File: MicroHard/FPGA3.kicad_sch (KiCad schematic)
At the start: 19 parts, among them J7 FPGA_DEBUG, U4 XC7A100T-FTG256

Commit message: Initial layout
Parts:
- renumbered R20 to R16, R22 to R17, R23 to R18, R24 to R19, R21 to R20, R16 to R21, R17 to R22, R18 to R23, R19 to R24, TP2 to TP1, TP1 to TP2
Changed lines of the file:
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@@
 		(dnp no)
 		(fields_autoplaced yes)
-		(property "Reference" "R22"
+		(property "Reference" "R17"
 			(at 177.8 55.8799 0)
 			(effects
@@
 			(project ""
 				(path "/578bd531-a491-4b15-a479-460d159ffc14/e381883e-e672-4900-88a5-08b94f970a88/5897012d-c01f-459a-b65a-eba111a7dafb"
-					(reference "R22")
+					(reference "R17")
 					(unit 1)
 				)
@@
 		(dnp no)
 		(fields_autoplaced yes)
-		(property "Reference" "R20"
+		(property "Reference" "R16"
 			(at 153.67 52.0699 0)
 			(effects
@@
 			(project ""
 				(path "/578bd531-a491-4b15-a479-460d159ffc14/e381883e-e672-4900-88a5-08b94f970a88/5897012d-c01f-459a-b65a-eba111a7dafb"
-					(reference "R20")
+					(reference "R16")
 					(unit 1)
 				)
@@
 		(dnp no)
 		(fields_autoplaced yes)
-		(property "Reference" "R23"
+		(property "Reference" "R18"
 			(at 237.49 57.1499 0)
 			(effects
@@
 			(project ""
 				(path "/578bd531-a491-4b15-a479-460d159ffc14/e381883e-e672-4900-88a5-08b94f970a88/5897012d-c01f-459a-b65a-eba111a7dafb"
-					(reference "R23")
+					(reference "R18")
 					(unit 1)
 				)
@@
 		(dnp no)
 		(fields_autoplaced yes)
-		(property "Reference" "R16"
+		(property "Reference" "R21"
 			(at 49.53 123.19 90)
 			(effects
@@
 			(project ""
 				(path "/578bd531-a491-4b15-a479-460d159ffc14/e381883e-e672-4900-88a5-08b94f970a88/5897012d-c01f-459a-b65a-eba111a7dafb"
-					(reference "R16")
+					(reference "R21")
 					(unit 1)
 				)
@@
 		(on_board yes)
 		(dnp no)
-		(property "Reference" "R19"
+		(property "Reference" "R24"
 			(at 52.324 152.908 90)
 			(effects
@@
 			(project "MicroHard"
 				(path "/578bd531-a491-4b15-a479-460d159ffc14/e381883e-e672-4900-88a5-08b94f970a88/5897012d-c01f-459a-b65a-eba111a7dafb"
-					(reference "R19")
+					(reference "R24")
 					(unit 1)
 				)
@@
 		(dnp no)
 		(fields_autoplaced yes)
-		(property "Reference" "#PWR035"
+		(property "Reference" "#PWR038"
 			(at 76.2 166.37 0)
 			(effects
@@
 			(project ""
 				(path "/578bd531-a491-4b15-a479-460d159ffc14/e381883e-e672-4900-88a5-08b94f970a88/5897012d-c01f-459a-b65a-eba111a7dafb"
-					(reference "#PWR035")
+					(reference "#PWR038")
 					(unit 1)
 				)
@@
 		(dnp no)
 		(fields_autoplaced yes)
-		(property "Reference" "#PWR034"
+		(property "Reference" "#PWR037"
 			(at 78.74 129.54 0)
 			(effects
@@
 			(project ""
 				(path "/578bd531-a491-4b15-a479-460d159ffc14/e381883e-e672-4900-88a5-08b94f970a88/5897012d-c01f-459a-b65a-eba111a7dafb"
-					(reference "#PWR034")
+					(reference "#PWR037")
 					(unit 1)
 				)
@@
 		(dnp no)
 		(fields_autoplaced yes)
-		(property "Reference" "#PWR038"
+		(property "Reference" "#PWR034"
 			(at 275.59 53.34 0)
 			(effects
@@
 			(project ""
 				(path "/578bd531-a491-4b15-a479-460d159ffc14/e381883e-e672-4900-88a5-08b94f970a88/5897012d-c01f-459a-b65a-eba111a7dafb"
-					(reference "#PWR038")
+					(reference "#PWR034")
 					(unit 1)
 				)
@@
 		(dnp no)
 		(fields_autoplaced yes)
-		(property "Reference" "R21"
+		(property "Reference" "R20"
 			(at 154.94 86.36 90)
 			(effects
@@
 			(project "MicroHard"
 				(path "/578bd531-a491-4b15-a479-460d159ffc14/e381883e-e672-4900-88a5-08b94f970a88/5897012d-c01f-459a-b65a-eba111a7dafb"
-					(reference "R21")
+					(reference "R20")
 					(unit 1)
 				)
@@
 		(dnp no)
 		(fields_autoplaced yes)
-		(property "Reference" "TP1"
+		(property "Reference" "TP2"
 			(at 151.13 76.9619 0)
 			(effects
@@
 			(project "MicroHard"
 				(path "/578bd531-a491-4b15-a479-460d159ffc14/e381883e-e672-4900-88a5-08b94f970a88/5897012d-c01f-459a-b65a-eba111a7dafb"
-					(reference "TP1")
+					(reference "TP2")
 					(unit 1)
 				)
@@
 		(on_board yes)
 		(dnp no)
-		(property "Reference" "R18"
+		(property "Reference" "R23"
 			(at 52.324 145.288 90)
 			(effects
@@
 			(project "MicroHard"
 				(path "/578bd531-a491-4b15-a479-460d159ffc14/e381883e-e672-4900-88a5-08b94f970a88/5897012d-c01f-459a-b65a-eba111a7dafb"
-					(reference "R18")
+					(reference "R23")
 					(unit 1)
 				)
@@
 		(dnp no)
 		(fields_autoplaced yes)
-		(property "Reference" "#PWR037"
+		(property "Reference" "#PWR035"
 			(at 125.73 63.5 0)
 			(effects
@@
 			(project ""
 				(path "/578bd531-a491-4b15-a479-460d159ffc14/e381883e-e672-4900-88a5-08b94f970a88/5897012d-c01f-459a-b65a-eba111a7dafb"
-					(reference "#PWR037")
+					(reference "#PWR035")
 					(unit 1)
 				)
@@
 		(dnp no)
 		(fields_autoplaced yes)
-		(property "Reference" "R24"
+		(property "Reference" "R19"
 			(at 247.65 57.1499 0)
 			(effects
@@
 			(project "MicroHard"
 				(path "/578bd531-a491-4b15-a479-460d159ffc14/e381883e-e672-4900-88a5-08b94f970a88/5897012d-c01f-459a-b65a-eba111a7dafb"
-					(reference "R24")
+					(reference "R19")
 					(unit 1)
 				)
@@
 		(on_board yes)
 		(dnp no)
-		(property "Reference" "R17"
+		(property "Reference" "R22"
 			(at 52.324 136.398 90)
 			(effects
@@
 			(project ""
 				(path "/578bd531-a491-4b15-a479-460d159ffc14/e381883e-e672-4900-88a5-08b94f970a88/5897012d-c01f-459a-b65a-eba111a7dafb"
-					(reference "R17")
+					(reference "R22")
 					(unit 1)
 				)
@@
 		(dnp no)
 		(fields_autoplaced yes)
-		(property "Reference" "TP2"
+		(property "Reference" "TP1"
 			(at 158.75 61.4679 0)
 			(effects
@@
 			(project "MicroHard"
 				(path "/578bd531-a491-4b15-a479-460d159ffc14/e381883e-e672-4900-88a5-08b94f970a88/5897012d-c01f-459a-b65a-eba111a7dafb"
-					(reference "TP2")
+					(reference "TP1")
 					(unit 1)
 				)

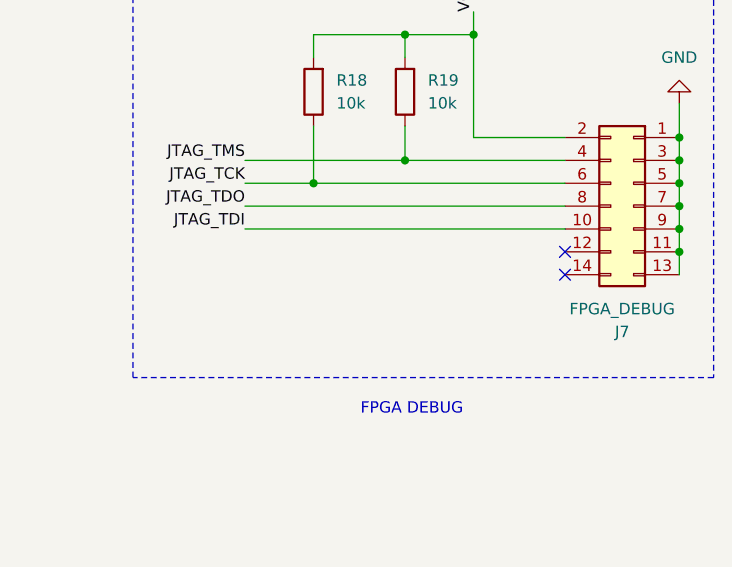
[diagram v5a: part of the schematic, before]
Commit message: power plane
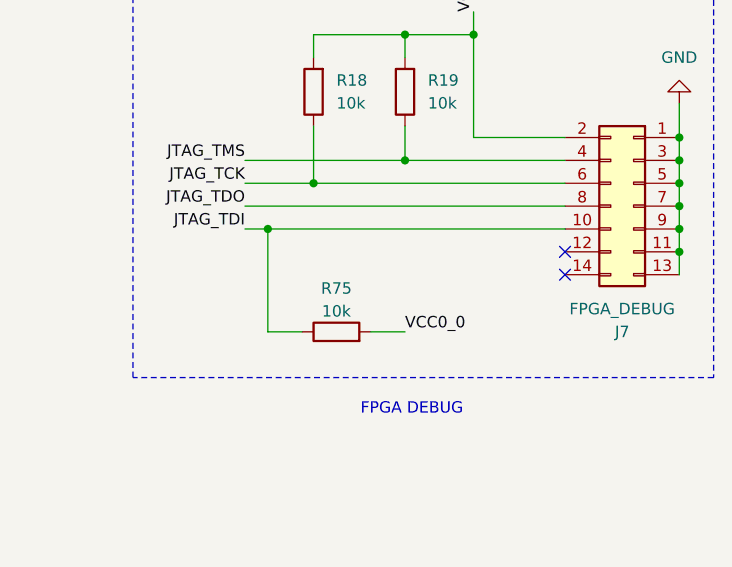
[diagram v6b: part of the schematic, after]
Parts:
- added R75: 10k, Resistor_SMD:R_1206_3216Metric_Pad1.30x1.75mm_HandSolder, symbol Device:R
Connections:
- net +3.3V: now also R75.2
- net JTAG_TDI: now also R75.1
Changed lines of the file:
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@@
+	)
+	(junction
+		(at 229.87 73.66)
+		(diameter 0)
+		(color 0 0 0 0)
 	)
 	(junction
@@
 	(wire
 		(pts
-			(xy 227.33 73.66) (xy 262.89 73.66)
+			(xy 227.33 73.66) (xy 229.87 73.66)
 		)
 		(stroke
@@
 	(wire
 		(pts
+			(xy 241.3 85.09) (xy 245.11 85.09)
+		)
+		(stroke
+			(width 0)
+			(type default)
+		)
+	)
+	(wire
+		(pts
 			(xy 252.73 49.53) (xy 252.73 52.07)
 		)
@@
 	(wire
 		(pts
+			(xy 229.87 73.66) (xy 262.89 73.66)
+		)
+		(stroke
+			(width 0)
+			(type default)
+		)
+	)
+	(wire
+		(pts
 			(xy 144.78 99.06) (xy 144.78 92.71)
 		)
@@
 	(wire
 		(pts
+			(xy 233.68 85.09) (xy 229.87 85.09)
+		)
+		(stroke
+			(width 0)
+			(type default)
+		)
+	)
+	(wire
+		(pts
 			(xy 38.1 129.54) (xy 45.72 129.54)
 		)
@@
 		(pts
 			(xy 58.42 129.54) (xy 53.34 129.54)
+		)
+		(stroke
+			(width 0)
+			(type default)
+		)
+	)
+	(wire
+		(pts
+			(xy 229.87 73.66) (xy 229.87 85.09)
 		)
 		(stroke
@@
 			)
 			(justify right bottom)
+		)
+	)
+	(label "VCC0_0"
+		(at 245.11 85.09 0)
+		(fields_autoplaced yes)
+		(effects
+			(font
+				(size 1.27 1.27)
+			)
+			(justify left bottom)
 		)
 	)
@@
 					(unit 1)
 				)
+			)
+		)
+	)
+	(symbol
+		(lib_id "Device:R")
+		(at 237.49 85.09 90)
+		(unit 1)
+		(exclude_from_sim no)
+		(in_bom yes)
+		(on_board yes)
+		(dnp no)
+		(property "Reference" "R75"
+			(at 237.49 80.264 90)
+			(effects
+				(font
+					(size 1.27 1.27)
+				)
+			)
+		)
+		(property "Value" "10k"
+			(at 237.49 82.804 90)
+			(effects
+				(font
+					(size 1.27 1.27)
+				)
+			)
+		)
+		(property "Footprint" "Resistor_SMD:R_1206_3216Metric_Pad1.30x1.75mm_HandSolder"
+			(at 237.49 86.868 90)
+			(effects
+				(font
+					(size 1.27 1.27)
+				)
+				(hide yes)
+			)
+		)
+		(property "Datasheet" "~"
+			(at 237.49 85.09 0)
+			(effects
+				(font
+					(size 1.27 1.27)
+				)
+				(hide yes)
+			)
+		)
+		(property "Description" "Resistor"
+			(at 237.49 85.09 0)
+			(effects
+				(font
+					(size 1.27 1.27)
+				)
+				(hide yes)
+			)
+		)
+		(property "Author" ""
+			(at 237.49 85.09 0)
+			(effects
+				(font
+					(size 1.27 1.27)
+				)
+				(hide yes)
+			)
+		)
+		(property "License" ""
+			(at 237.49 85.09 0)
+			(effects
+				(font
+					(size 1.27 1.27)
+				)
+				(hide yes)
+			)
+		)
+		(property "MPN" ""
+			(at 237.49 85.09 0)
+			(effects
+				(font
+					(size 1.27 1.27)
+				)
+				(hide yes)
+			)
+		)
+		(property "Manufacturer" ""
+			(at 237.49 85.09 0)
+			(effects
+				(font
+					(size 1.27 1.27)
+				)
+				(hide yes)
+			)
+		)
+		(property "Tolerance" ""
+			(at 237.49 85.09 0)
+			(effects
+				(font
+					(size 1.27 1.27)
+				)
+				(hide yes)
+			)
+		)
+		(property "Val" ""
+			(at 237.49 85.09 0)
+			(effects
+				(font
+					(size 1.27 1.27)
+				)
+				(hide yes)
+			)
+		)
+		(pin "1"
+		)
+		(pin "2"
+		)
+		(instances
+			(project "MicroHard"
+				(path "/578bd531-a491-4b15-a479-460d159ffc14/e381883e-e672-4900-88a5-08b94f970a88/5897012d-c01f-459a-b65a-eba111a7dafb"
+					(reference "R75")
+					(unit 1)
+				)

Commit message: Fix schematics for delivery
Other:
- company: (none) -> MicroHard
- title: (none) -> FPGA Config
